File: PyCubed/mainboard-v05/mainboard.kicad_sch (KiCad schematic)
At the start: 0 parts

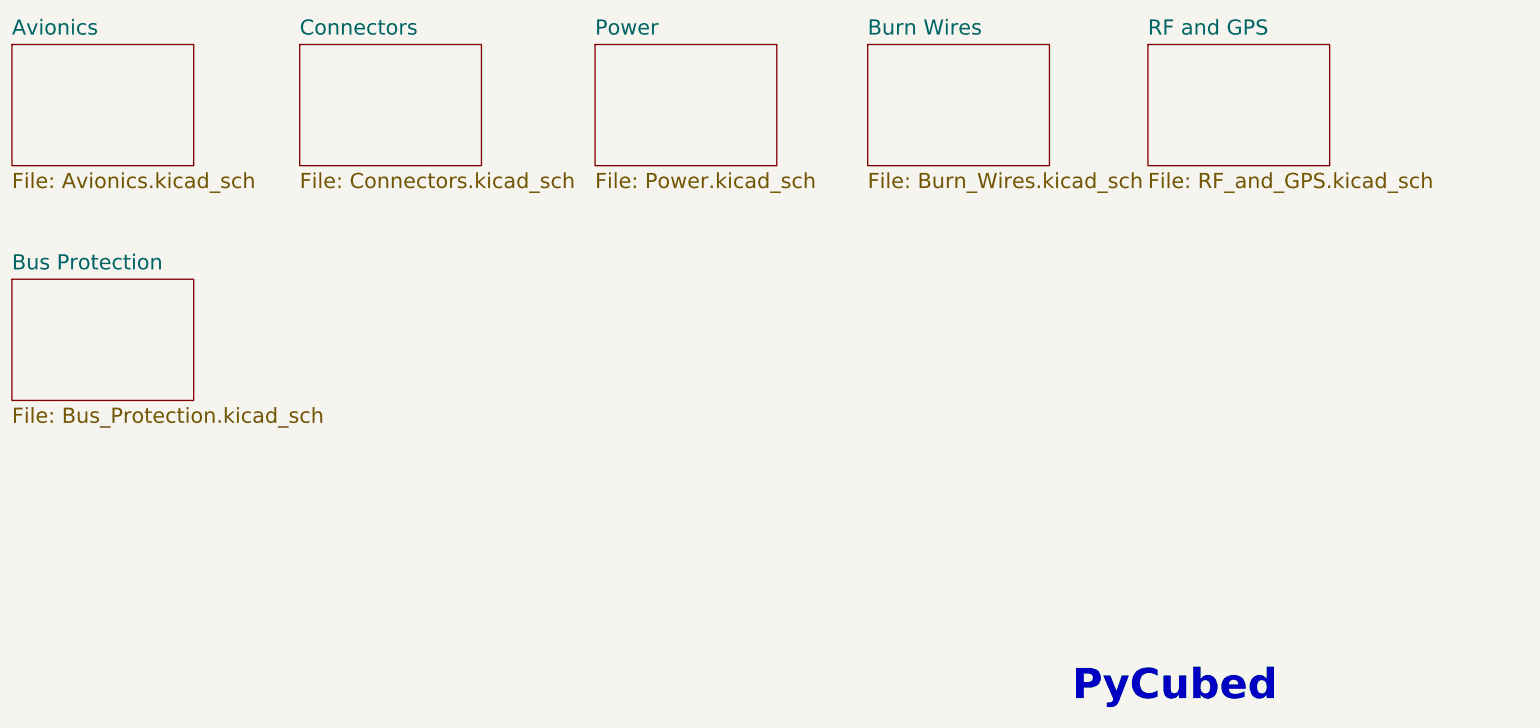
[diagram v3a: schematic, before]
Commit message: add replacement sensors
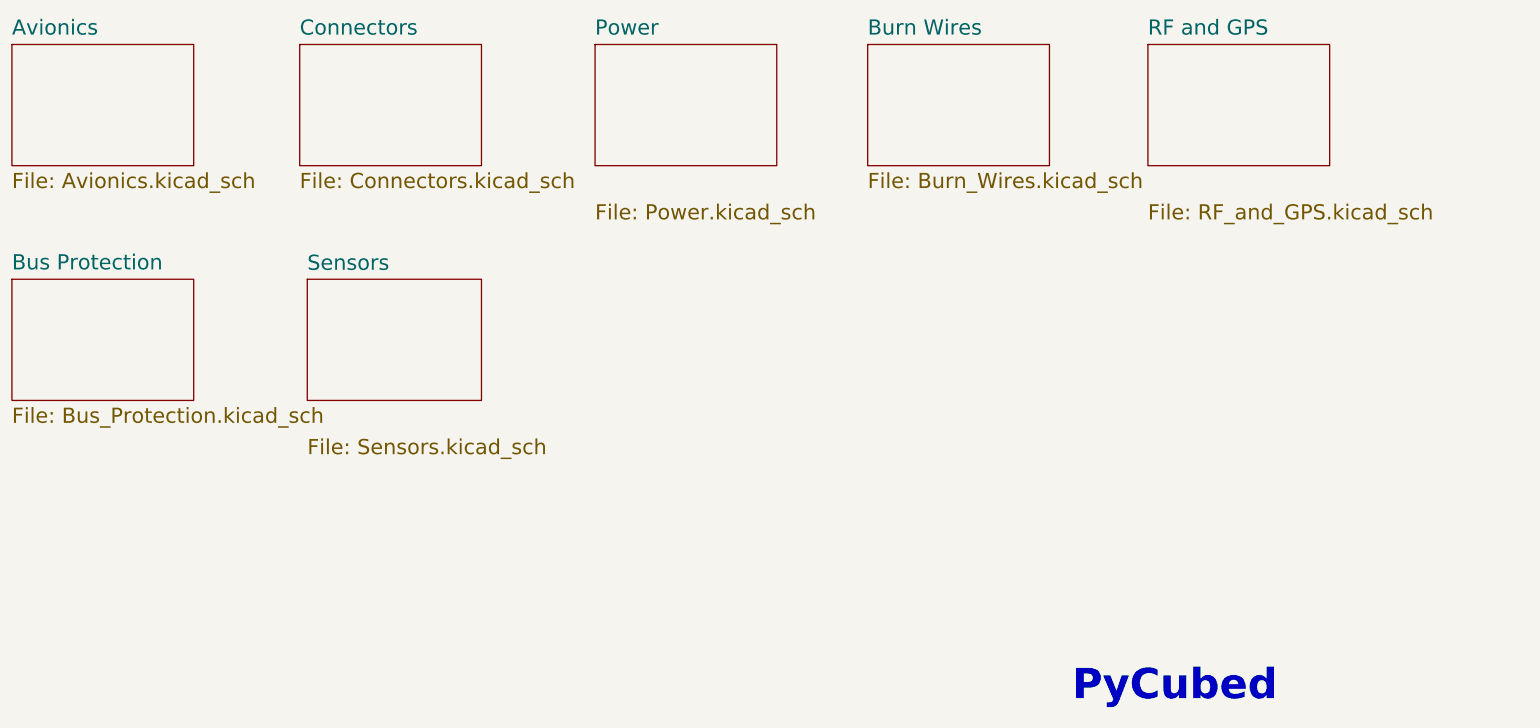
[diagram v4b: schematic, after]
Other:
- added sheet Sensors (Sensors.kicad_sch)
